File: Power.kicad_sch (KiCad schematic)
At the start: 11 parts, among them J7 USB_C_Receptacle_USB2.0_14P, U4 AP63205WU, U5 MCP1802x-xx02xOT

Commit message: Rev1. Uart interface
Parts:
- removed J7: USB_C_Receptacle_USB2.0_14P, Connector_USB:USB_C_Receptacle_GCT_USB4085, symbol Connector:USB_C_Receptacle_USB2.0_14P
- removed R17, R20: 5.1k, Resistor_SMD:R_0805_2012Metric, symbol Device:R_US
- added C15, C16: 1uF, Capacitor_SMD:C_0805_2012Metric, symbol Device:C
- added C17: 4.7uF, Capacitor_SMD:C_0805_2012Metric, symbol Device:C
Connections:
- net +3.3V: now also C15.1, C16.1
- net +5V: now also C17.1
- net GND: now also C15.2, C16.2, C17.2
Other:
- note added: "The 3 fans will draw 0.64A. MCU seems to draw max 23mA. Total 3.32W. Including 40W heater and 0.3A motor, whole board should draw 2.1A max."
- note added: "Use LP5907?"

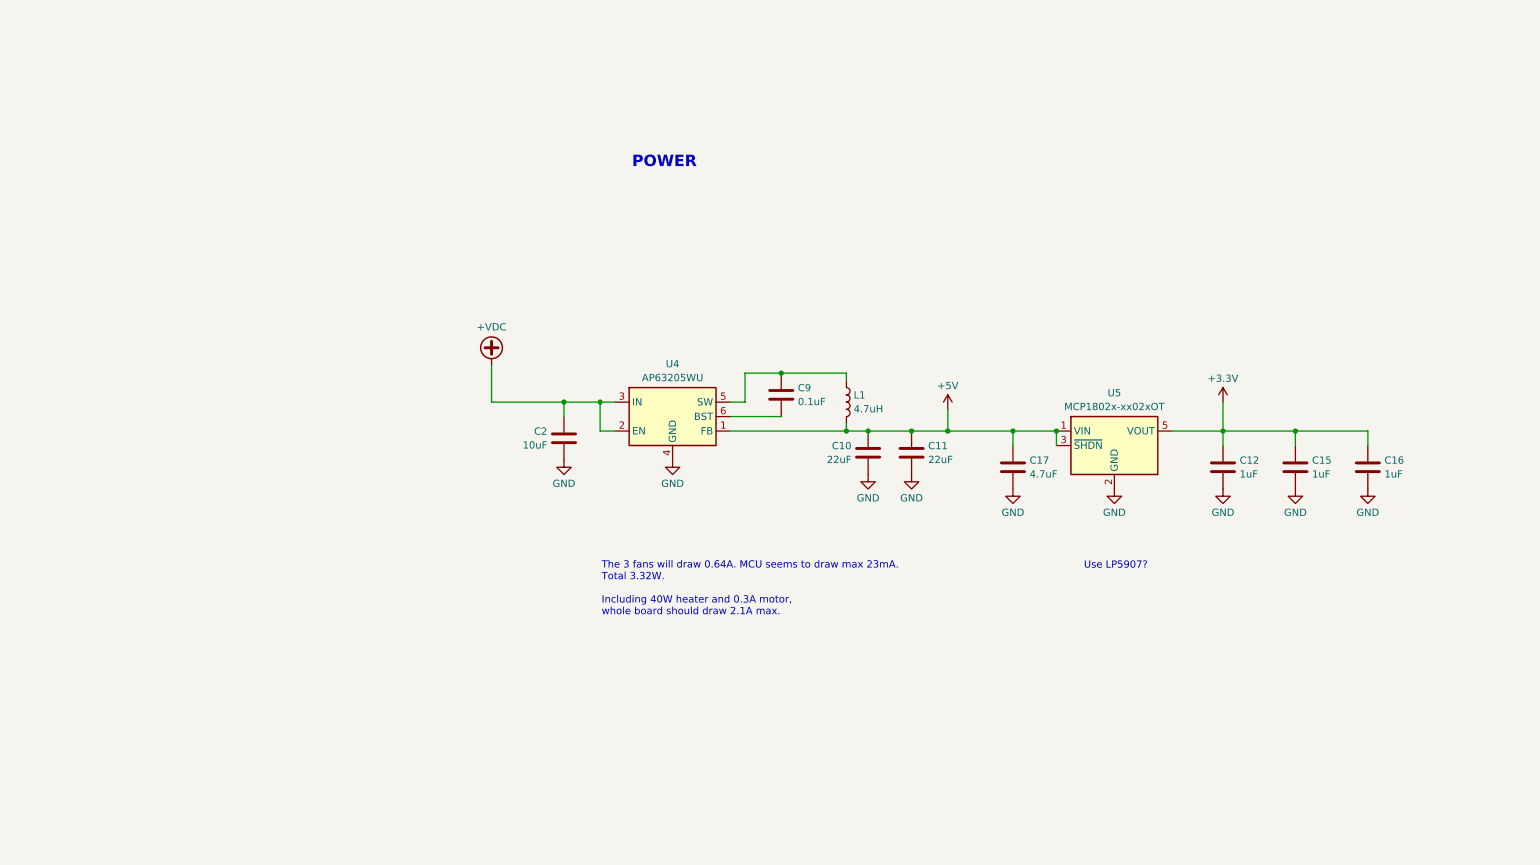
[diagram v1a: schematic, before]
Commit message: Rev2 (USB) largely done
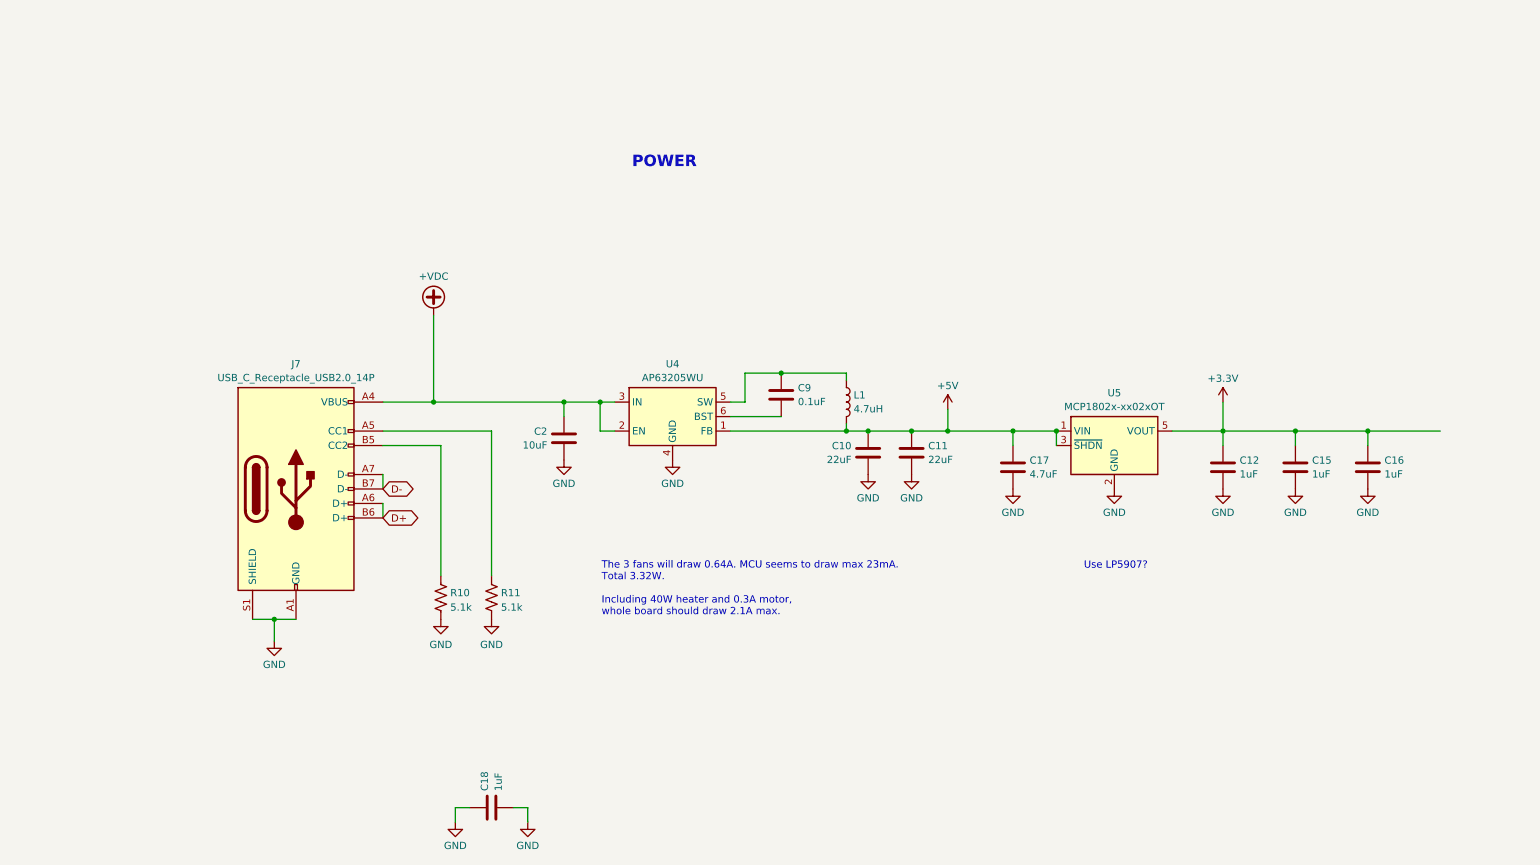
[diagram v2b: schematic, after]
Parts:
- added C18: 1uF, Capacitor_SMD:C_0805_2012Metric, symbol Device:C
- added J7: USB_C_Receptacle_USB2.0_14P, symbol Connector:USB_C_Receptacle_USB2.0_14P
- added R10, R11: 5.1k, Resistor_SMD:R_0805_2012Metric, symbol Device:R_US
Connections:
- net +VDC: now also J7.A4 (VBUS), J7.A9 (VBUS), J7.B4 (VBUS), J7.B9 (VBUS)
- net GND: now also C18.1, C18.2, J7.A1 (GND), J7.A12 (GND), J7.B1 (GND), J7.B12 (GND), J7.S1 (SHIELD), R10.2, R11.2
- new net: J7.A5 (CC1), R11.1
- new net: J7.B5 (CC2), R10.1
- new net D+: J7.A6 (D+), J7.B6 (D+)
- new net D-: J7.A7 (D-), J7.B7 (D-)

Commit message: Rev2, as ordered
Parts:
- removed R10, R11: 5.1k, Resistor_SMD:R_0805_2012Metric, symbol Device:R_US
- added C19: 4.7uF, Capacitor_SMD:C_0805_2012Metric, symbol Device:C
- added C20: 1uF, Capacitor_SMD:C_0603_1608Metric, symbol Device:C
- added U6: LP5907-2.5, Package_TO_SOT_SMD:SOT-23-5, symbol Regulator_Linear:MCP1802x-xx02xOT
- C12, C15, C16, C18: footprint Capacitor_SMD:C_0805_2012Metric -> Capacitor_SMD:C_0603_1608Metric
- J7: footprint (none) -> Connector_USB:USB_C_Receptacle_GCT_USB4085
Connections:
- net +5V: now also C19.1, U6.1 (VIN), U6.3 (~{SHDN})
- net GND: now also C19.2, C20.2, U6.2 (GND)
- new net +2V5: C20.1, U6.5 (VOUT)
- no-connect marks 0 -> 2
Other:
- moved on the sheet: C10, C11, C12, C15, C16, C17, C18, C2, C9, J7, L1, U4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

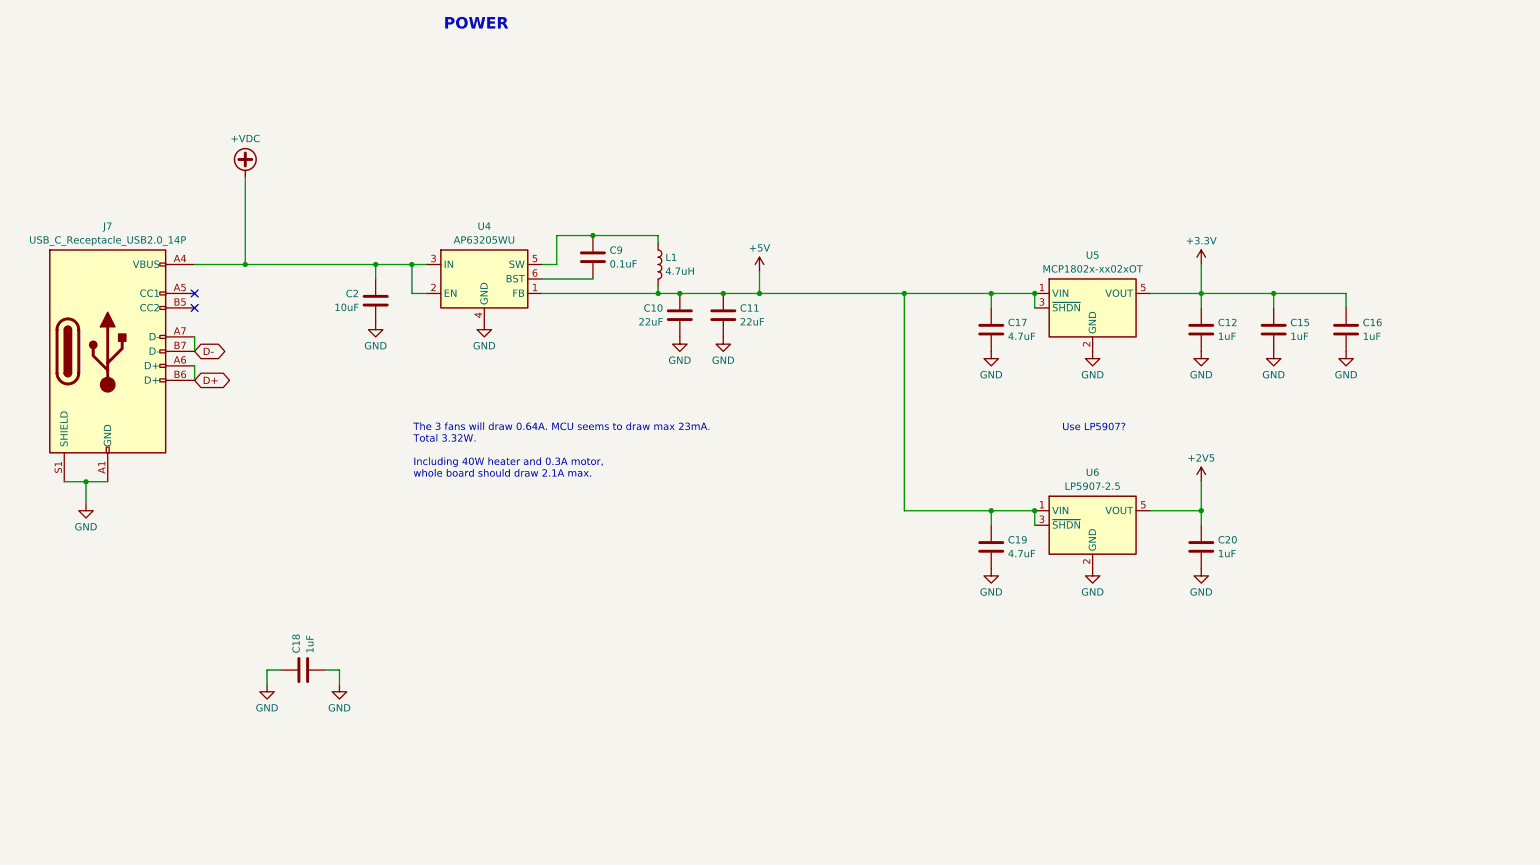
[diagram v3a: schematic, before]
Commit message: Rev3 (connectors on back, and with USB daughter board) - probably done
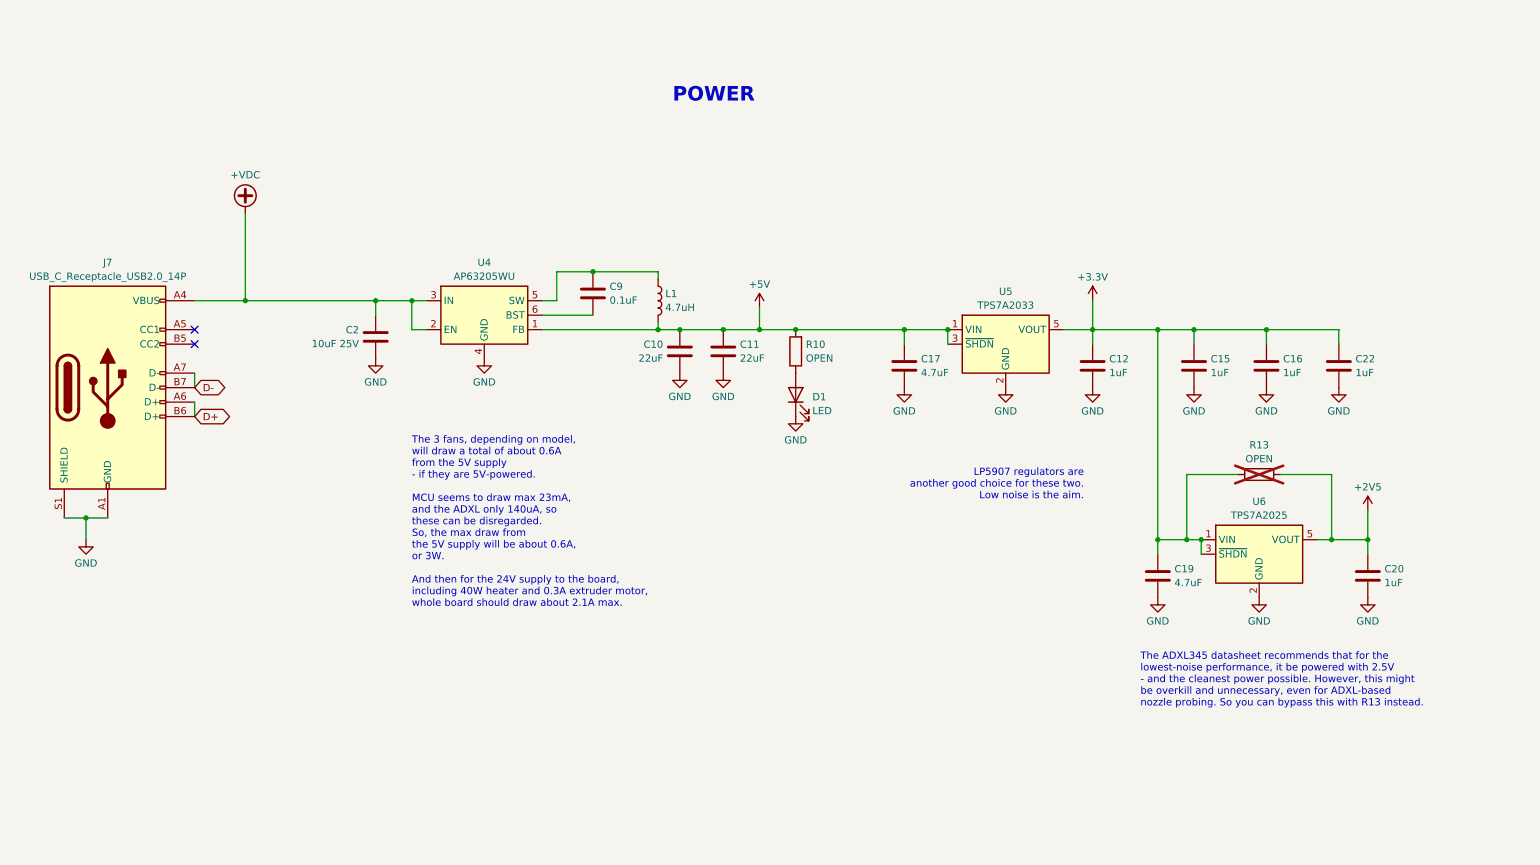
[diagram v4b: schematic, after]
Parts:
- removed C18: 1uF, Capacitor_SMD:C_0603_1608Metric, symbol Device:C
- added C22: 1uF, Capacitor_SMD:C_0603_1608Metric, symbol Device:C
- added D1: LED, LED_SMD:LED_0603_1608Metric, symbol Device:LED
- added R10, R13: OPEN, Resistor_SMD:R_0603_1608Metric, symbol Device:R
- C2: value 10uF -> 10uF 25V
- C9: footprint Capacitor_SMD:C_0805_2012Metric -> Capacitor_SMD:C_0603_1608Metric
- U5: value MCP1802x-xx02xOT -> TPS7A2033
- U6: value LP5907-2.5 -> TPS7A2025
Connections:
- net +2V5: now also R13.2
- net +3.3V: now also C19.1, U6.1 (VIN), U6.3 (~{SHDN}), C22.1, R13.1
- net +5V: now also R10.2; no longer C19.1, U6.1 (VIN), U6.3 (~{SHDN})
- net GND: now also C22.2, D1.1 (K)
- new net: D1.2 (A), R10.1
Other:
- note added: "LP5907 regulators are another good choice for these two. Low noise is the aim."
- note added: "The 3 fans, depending on model, will draw a total of about 0.6A from the 5V supply - if they are 5V-powered. MCU seems to draw max 23mA, and the ADXL only 140uA, so these can be disregarded. So, the max draw from the 5V supply will be about 0.6A, or 3W. And then for the 24V supply to the board, including 40W heater and 0.3A extruder motor, whole board should draw about 2.1A max."
- note added: "The ADXL345 datasheet recommends that for the lowest-noise performance, it be powered with 2.5V - and the cleanest power possible. However, this might be overkill and unnecessary, even for ADXL-based nozzle probing. So you can bypass this with R13 instead."
- note removed: "The 3 fans will draw 0.64A. MCU seems to draw max 23mA. Total 3.32W. Including 40W heater and 0.3A motor, whole board should draw 2.1A max."
- note removed: "Use LP5907?"
- moved on the sheet: C10, C11, C12, C15, C16, C17, C19, C2, C20, C9, J7, L1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

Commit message: Little changes while populating
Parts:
- R10: value OPEN -> 22k
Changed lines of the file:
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@@
 			)
 		)
-		(property "Value" "OPEN"
+		(property "Value" "22k"
 			(at 161.798 81.2221 0)
 			(effects
